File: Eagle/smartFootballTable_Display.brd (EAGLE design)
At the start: 55.9 x 53.3 mm, 13 parts, among them SW3 DIP-6X_DIP

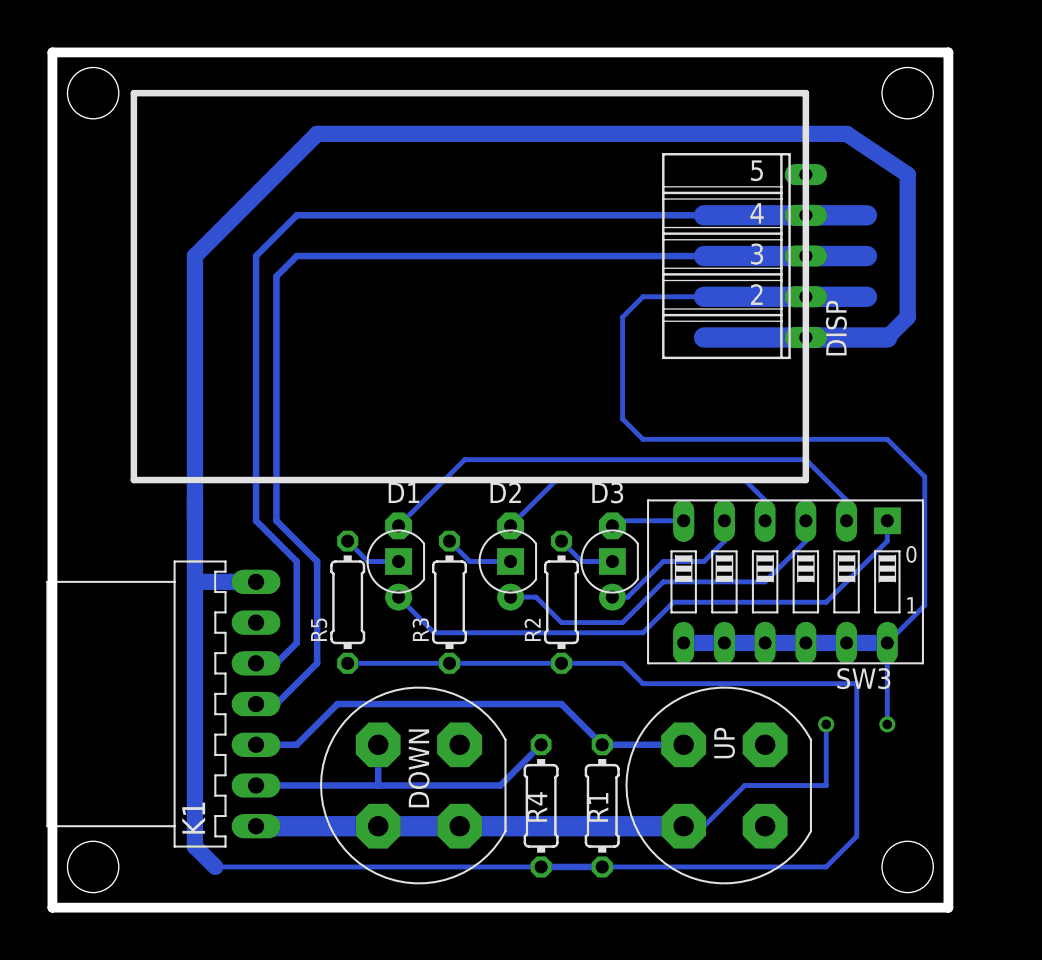
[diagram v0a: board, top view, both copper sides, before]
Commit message: Made changes for the display board before fabrication
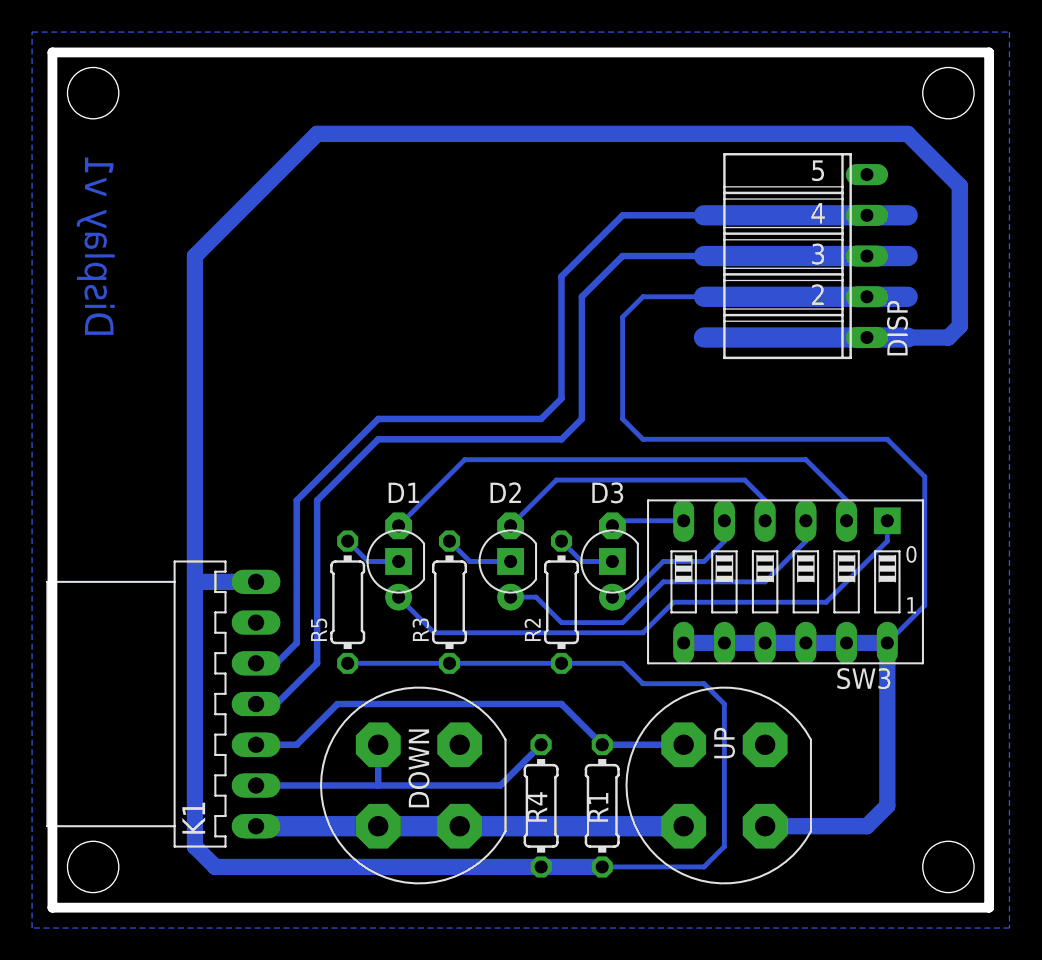
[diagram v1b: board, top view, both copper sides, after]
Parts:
- moved DISP 3.81 mm to (50.8, 40.6)
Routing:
- net GND: track 200.6 -> 185.3 mm
- net VCC: track 112.0 -> 122.6 mm
- net CLK: track 67.4 -> 61.9 mm
- net DIO: track 67.4 -> 63.9 mm
- added copper zone on layer 16, net GND
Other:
- board size 55.9 x 53.3 mm -> 58.4 x 53.3 mm
- board text added: "Display v1"
